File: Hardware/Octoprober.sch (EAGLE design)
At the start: 167 parts, among them J1 10118193-0001LF, SW1 EVQ-Q2203W, SW2 EVQ-Q2203W, SW3 EVQ-Q2203W, SW4 EVQ-Q2203W, SW5 EVQ-Q2203W, U1 P8X32A-M44, U10 DS1340Z-33+, U11 MCP3424-E/ST, U12 MCP3424-E/ST, U13 AT30TSE752-XM8-T, U14 AT30TSE752-XM8-T, U15 AT30TSE752-XM8-T, U16 AT30TSE752-XM8-T, U17 AT30TSE752-XM8-T, U18 AT30TSE752-XM8-T, U19 AT30TSE752-XM8-T, U2 CAT24C512WI-GT3, U20 AT30TSE752-XM8-T, U21 PMV22EN,215, U3 ADP3338AKCZ-3.3-RL, U4 FT230XQ-R, U5 BQ24075RGTT, U6 74HC2G04GV,125, U7 PMV22EN,215, U8 PMV160UP,215, U9 MCP3021A5T-E/OT, X1 ABLS3-6.000MHZ-D4Y-T, X2 ABS25-32.768KHz-1-T

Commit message: New chips for thermocouples.
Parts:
- removed C54: 1uF, PP_Passives:CAPACITOR_NON_POLAR0402
- removed FU: (no value), PP_Connectors:PH_1X09PTH
- removed J1: 10118193-0001LF, PP_Connectors:USB10118193-0001LF
- removed L10, L11, L12, L13, L14, L15, L16, L17, L3, L4, L5, L6, L7, L8, L9: BK1005HM471-T, PP_Passives:INDUCTOR0402
- removed LCD1: (no value), PP_Displays:HD44780_LCD1602_COUNTERSINK
- removed R36: 10K, PP_Passives:RESISTOR0402
- removed R37, R38: 560, PP_Passives:RESISTOR0402
- removed U20: AT30TSE752-XM8-T, PP_DigitalIC:AT30TSEXXXMSOP-8
- removed U21: PMV22EN,215, PP_DiscreteSemi:MOSFET_N-CHANNEL_SINGLESOT-23
- added C55, C58, C59, C60, C63, C64, C65, C68, C69, C70, C73, C74: 0.1uF, PP_Passives:CAPACITOR_NON_POLAR0402
- added C56, C57, C61, C62, C66, C67, C71, C72: 0.01uF, PP_Passives:CAPACITOR_NON_POLAR0402
- added FID1: GSM_FIDUCIAL, MF_Aesthetics:GSM_FIDUCIAL
- added J3: (no value), MF_Connectors:USB_MICRO_RIGHT
- added U$7: MF_LOGOLOGO_MEDIUM, PP_Aesthetics:MF_LOGOLOGO_MEDIUM
- C10, C11, C12, C13, C14, C2, C3, C34, C37, C38, C39, C4, C40, C5, C6, C9: device PP_Passives:CAPACITOR_NON_POLAR0402 -> PP_Passives:CAPACITOR_NON_POLAR0603
- C15, C21, C29, C49, C50: value 0.1uF -> 0.01uF
- C16, C18, C20, C24, C26, C28: value 0.01uF -> 0.1uF
- C17: value 10uF -> 0.01uF
- C19: value 10uF -> 0.1uF
- C41, C42, C43, C44: device PP_Passives:CAPACITOR_NON_POLAR0402 -> PP_Passives:CAPACITOR_NON_POLAR1206
- D1, D12, D2: device PP_LED:LED_SINGLE0402 -> PP_LED:LED_SINGLE0805
- L2: value BK1005HM471-T -> MI0603K300R-10; device PP_Passives:INDUCTOR0402 -> PP_Passives:RESISTOR0603
- R1, R10, R11, R12, R13, R14, R15, R16, R17, R18, R19, R20, R21, R22, R23, R24, R25, R26, R27, R28, R29, R30, R31, R32, R33, R34, R8, R9: device PP_Passives:RESISTOR0402 -> PP_Passives:RESISTOR0603
- SD1: value 502570-0893 -> (none); device PP_Connectors:SD_CARD502570-0893 -> MF_Connectors:SD_CARD_SLOT_MICRO_RIGHT
- U$1: REVNUM REV 2 -> REV 3
- U1: value P8X32A-M44 -> P8X32A-Q44; device PP_DigitalIC:P8X32A_PROPELLERQFN-44 -> MF_IC_Digital:P8X32A-Q44
- U11, U12: value MCP3424-E/ST -> MAX31856MUD+; device PP_DigitalIC:MCP3424TTSOP-14 -> PP_AnalogIC:MAX31856
- U13, U14, U15, U16, U17, U18: value AT30TSE752-XM8-T -> MAX31856MUD+; device PP_DigitalIC:AT30TSEXXXMSOP-8 -> PP_AnalogIC:MAX31856
- U19: value AT30TSE752-XM8-T -> IP4234CZ6,125; device PP_DigitalIC:AT30TSEXXXMSOP-8 -> PP_Passives:IP4234CZ6SOT-457
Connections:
- removed net LCD_CS: LCD1.BK_GND, U1.P7
- removed net LCD_SDI: LCD1.D7, U1.P6
- removed net LCD_SDO: LCD1.D6, U1.P5
- removed net N$10: D6.2, L7.P$1, TC3.2
- removed net N$11: D6.1, L6.P$2, TC3.1
- removed net N$12: D7.2, L9.P$1, TC4.2
- removed net N$13: D7.1, L8.P$2, TC4.1
- removed net N$14: D11.2, L17.P$1, TC8.2
- removed net N$15: D11.1, L16.P$2, TC8.1
- removed net N$16: D10.2, L15.P$1, TC7.2
- removed net N$17: D10.1, L14.P$2, TC7.1
- removed net N$18: D9.2, L13.P$1, TC6.2
- removed net N$19: D9.1, L12.P$2, TC6.1
- removed net N$2: D4.2, L2.P$1, TC1.2
- removed net N$20: D8.2, L11.P$1, TC5.2
- removed net N$21: D8.1, L10.P$2, TC5.1
- removed net N$28: R37.1, U21.DRAIN
- removed net N$7: D4.1, L3.P$2, TC1.1
- removed net N$8: D5.2, L5.P$1, TC2.2
- removed net N$9: D5.1, L4.P$2, TC2.1
- removed net P12: FU.3, U1.P12
- removed net P13: FU.4, U1.P13
- removed net P14: FU.5, U1.P14
- removed net P15: FU.6, U1.P15
- removed net P16: FU.7, U1.P16
- removed net P17: FU.8, U1.P17
- removed net P18: FU.9, U1.P18
- removed net SCL_ADC: U1.P9, U11.SCL, U12.SCL, U13.SCL, U14.SCL, U15.SCL, U16.SCL, U17.SCL, U18.SCL, U19.SCL, U20.SCL
- removed net SDA_ADC: U1.P10, U11.SDA, U12.SDA, U13.SDA, U14.SDA, U15.SDA, U16.SDA, U17.SDA, U18.SDA, U19.SDA, U20.SDA
- removed net SHT_DRAIN: R36.1, U1.P11, U21.GATE
- new net ADC_0_!CS: U1.P12, U11.!CS
- new net ADC_1_!CS: U1.P13, U12.!CS
- new net ADC_2_!CS: U1.P14, U13.!CS
- new net ADC_3_!CS: U1.P15, U14.!CS
- new net ADC_4_!CS: U1.P16, U15.!CS
- new net ADC_5_!CS: U1.P17, U16.!CS
- new net ADC_6_!CS: U1.P18, U17.!CS
- new net ADC_7_!CS: U1.P19, U18.!CS
- new net ADC_SCK: U1.P11, U11.SCK, U12.SCK, U13.SCK, U14.SCK, U15.SCK, U16.SCK, U17.SCK, U18.SCK
- new net ADC_SDI: U1.P9, U11.SDI, U12.SDI, U13.SDI, U14.SDI, U15.SDI, U16.SDI, U17.SDI, U18.SDI
- new net ADC_SDO: U1.P10, U11.SDO, U12.SDO, U13.SDO, U14.SDO, U15.SDO, U16.SDO, U17.SDO, U18.SDO
- new net LCD_SDA: U1.P5
- new net N$23: J3.D-, U19.I/O2A
- new net N$26: J3.D+, U19.I/O1A
- new net N$27: J3.SLD, L2.1
- new net P6: U1.P6
- new net P7: U1.P7
- net !SLEEP: no longer U1.P20
- net 3.3V: no longer C54.2, FU.1, LCD1.VCC, R36.2, R37.2, R38.1
- net 3.3V_ANALOG: now also C18.1, C24.1, C26.1, C46.1, C47.1, C51.1, C52.1, C58.1, C59.1, C63.1, C64.1, C68.1, C69.1, C73.1, C74.1, U11.AVDD, U11.DVDD, U12.AVDD, U12.DVDD, U13.AVDD, U13.DVDD, U14.AVDD, U14.DVDD, U15.AVDD, U15.DVDD, U16.AVDD, U16.DVDD, U17.AVDD, U17.DVDD, U18.AVDD, U18.DVDD; no longer C15.1, C17.1, C21.1, C29.2, C46.2, C47.2, C48.2, C49.2, C50.2, C51.2, C52.2, U11.VCC, U12.ADR0, U12.ADR1, U12.VCC, U13.VCC, U14.A0, U14.VCC, U15.A1, U15.VCC, U16.A0, U16.A1, U16.VCC, U17.A2, U17.VCC, U18.A0, U18.A2, U18.VCC, U19.A1, U19.A2, U19.VCC, U20.A0, U20.A1, U20.A2, U20.VCC
- net CHARGING: now also U1.P20; no longer U1.P19
- net D+: now also U19.I/O1B; no longer J1.D+
- net D-: now also U19.I/O2B; no longer J1.D-
- net GND: now also C18.2, C22.2, C24.2, C26.2, C29.2, C30.2, C46.2, C47.2, C49.2, C50.2, C51.2, C52.2, C56.2, C57.2, C58.2, C59.2, C61.2, C62.2, C63.2, C64.2, C66.2, C67.2, C68.2, C69.2, C71.2, C72.2, C73.2, C74.2, J3.GND, L2.2, U11.AGND, U11.DGND, U12.AGND, U12.DGND, U13.AGND, U13.DGND, U14.AGND, U14.DGND, U15.AGND, U15.DGND, U16.AGND, U16.DGND, U17.AGND, U17.DGND, U18.AGND, U18.DGND; no longer C29.1, C46.1, C47.1, C48.1, C49.1, C50.1, C51.1, C52.1, C54.1, FU.2, J1.GND, LCD1.VSS, R38.2, U11.ADR0, U11.ADR1, U11.VDD, U12.VDD, U13.A0, U13.A1, U13.A2, U13.GND, U14.A1, U14.A2, U14.GND, U15.A0, U15.A2, U15.GND, U16.A2, U16.GND, U17.A0, U17.A1, U17.GND, U18.A1, U18.GND, U19.A0, U20.GND, U21.SOURCE
- net LCD_SCL: no longer LCD1.D5
- net TP_T+_0: now also C17.1, D4.1, TC1.1, U11.T+; no longer L3.P$1, U11.CH1+
- net TP_T+_1: now also C20.2, C22.1, D5.1, TC2.1, U12.T+; no longer C18.2, L4.P$1, U11.CH2+
- net TP_T+_2: now also C28.2, C30.1, D6.1, TC3.1, U13.T+; no longer C20.2, L6.P$1, U11.CH3+
- net TP_T+_3: now also C48.2, C50.1, D7.1, TC4.1, U14.T+; no longer C22.2, L8.P$1, U11.CH4+
- net TP_T+_4: now also C55.2, C57.1, D8.1, TC5.1, U15.T+; no longer C24.2, L10.P$1, U12.CH1+
- net TP_T+_5: now also C60.2, C62.1, D9.1, TC6.1, U16.T+; no longer C26.2, L12.P$1, U12.CH2+
- net TP_T+_6: now also C65.2, C67.1, D10.1, TC7.1, U17.T+; no longer C28.2, L14.P$1, U12.CH3+
- net TP_T+_7: now also C70.2, C72.1, D11.1, TC8.1, U18.T+; no longer C30.2, L16.P$1, U12.CH4+
- net TP_T-_0: now also C15.1, D4.2, TC1.2, U11.BIAS, U11.T-; no longer L2.P$2, U11.CH1-
- net TP_T-_1: now also C20.1, C21.1, D5.2, TC2.2, U12.BIAS, U12.T-; no longer C18.1, L5.P$2, U11.CH2-
- net TP_T-_2: now also C28.1, C29.1, D6.2, TC3.2, U13.BIAS, U13.T-; no longer C20.1, L7.P$2, U11.CH3-
- net TP_T-_3: now also C48.1, C49.1, D7.2, TC4.2, U14.BIAS, U14.T-; no longer C22.1, L9.P$2, U11.CH4-
- net TP_T-_4: now also C55.1, C56.1, D8.2, TC5.2, U15.BIAS, U15.T-; no longer C24.1, L11.P$2, U12.CH1-
- net TP_T-_5: now also C60.1, C61.1, D9.2, TC6.2, U16.BIAS, U16.T-; no longer C26.1, L13.P$2, U12.CH2-
- net TP_T-_6: now also C65.1, C66.1, D10.2, TC7.2, U17.BIAS, U17.T-; no longer C28.1, L15.P$2, U12.CH3-
- net TP_T-_7: now also C70.1, C71.1, D11.2, TC8.2, U18.BIAS, U18.T-; no longer C30.1, L17.P$2, U12.CH4-
- net USB_V0: now also J3.5V, U19.VB; no longer J1.5V
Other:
- moved on the sheet: C15, C16, C17, C18, C19, C20, C21, C22, C24, C26, C28, C29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

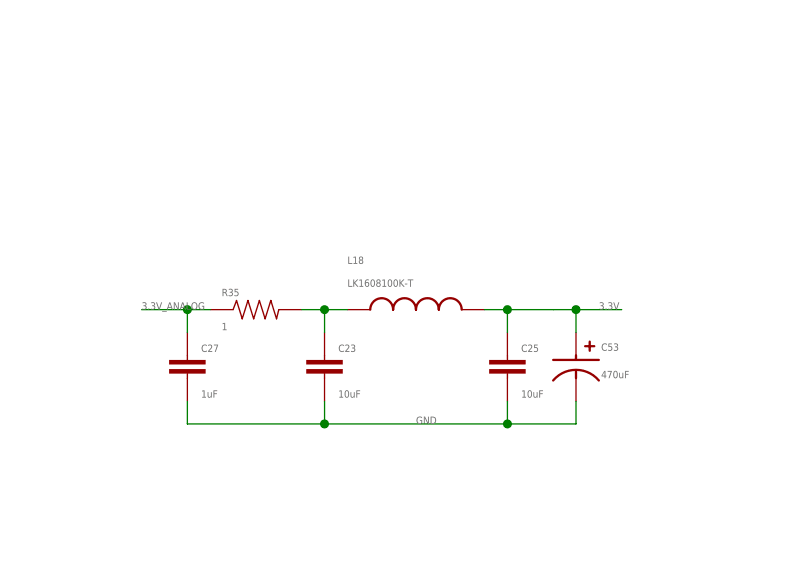
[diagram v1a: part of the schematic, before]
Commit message: Working on LCD setup. Need to find a case.
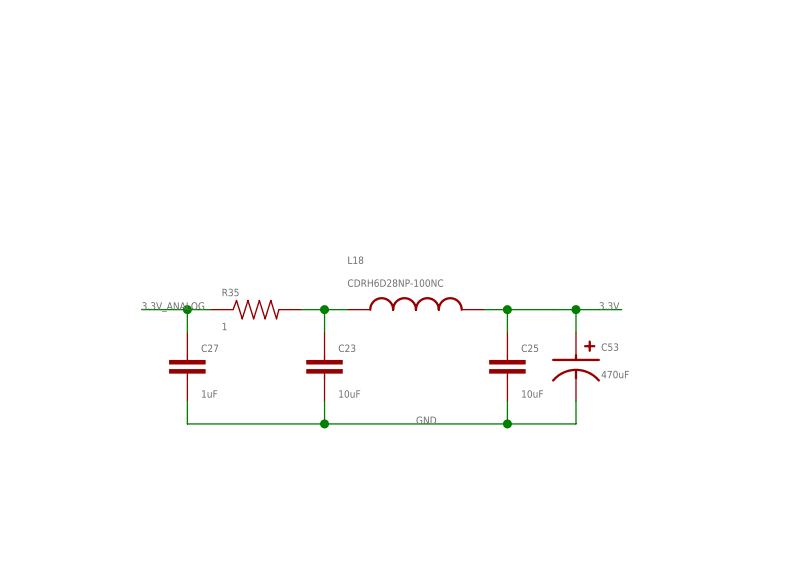
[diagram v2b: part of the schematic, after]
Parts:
- C23, C25: device PP_Passives:CAPACITOR_NON_POLAR0402 -> PP_Passives:CAPACITOR_NON_POLAR1206
- C27: device PP_Passives:CAPACITOR_NON_POLAR0402 -> PP_Passives:CAPACITOR_NON_POLAR0603
- L18: value LK1608100K-T -> CDRH6D28NP-100NC; device PP_Passives:INDUCTOR0603 -> PP_Passives:INDUCTORCDRH6D28
- R35: device PP_Passives:RESISTOR0402 -> PP_Passives:RESISTOR0603
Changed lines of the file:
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@@
 <part name="C44" library="PP_Passives" deviceset="CAPACITOR_NON_POLAR" device="1206" value="10uF"/>
 <part name="C45" library="PP_Passives" deviceset="CAPACITOR_POLARIZED" device="CASE_D" value="470uF"/>
-<part name="C23" library="PP_Passives" deviceset="CAPACITOR_NON_POLAR" device="0402" value="10uF"/>
-<part name="C25" library="PP_Passives" deviceset="CAPACITOR_NON_POLAR" device="0402" value="10uF"/>
-<part name="C27" library="PP_Passives" deviceset="CAPACITOR_NON_POLAR" device="0402" value="1uF"/>
-<part name="R35" library="PP_Passives" deviceset="RESISTOR" device="0402" value="1"/>
-<part name="L18" library="PP_Passives" deviceset="INDUCTOR" device="0603" value="LK1608100K-T"/>
+<part name="C23" library="PP_Passives" deviceset="CAPACITOR_NON_POLAR" device="1206" value="10uF"/>
+<part name="C25" library="PP_Passives" deviceset="CAPACITOR_NON_POLAR" device="1206" value="10uF"/>
+<part name="C27" library="PP_Passives" deviceset="CAPACITOR_NON_POLAR" device="0603" value="1uF"/>
+<part name="R35" library="PP_Passives" deviceset="RESISTOR" device="0603" value="1"/>
+<part name="L18" library="PP_Passives" deviceset="INDUCTOR" device="CDRH6D28" value="CDRH6D28NP-100NC"/>
 <part name="C53" library="PP_Passives" deviceset="CAPACITOR_POLARIZED" device="CASE_D" value="470uF"/>
 <part name="U11" library="PP_AnalogIC" deviceset="MAX31856" device="" value="MAX31856MUD+"/>

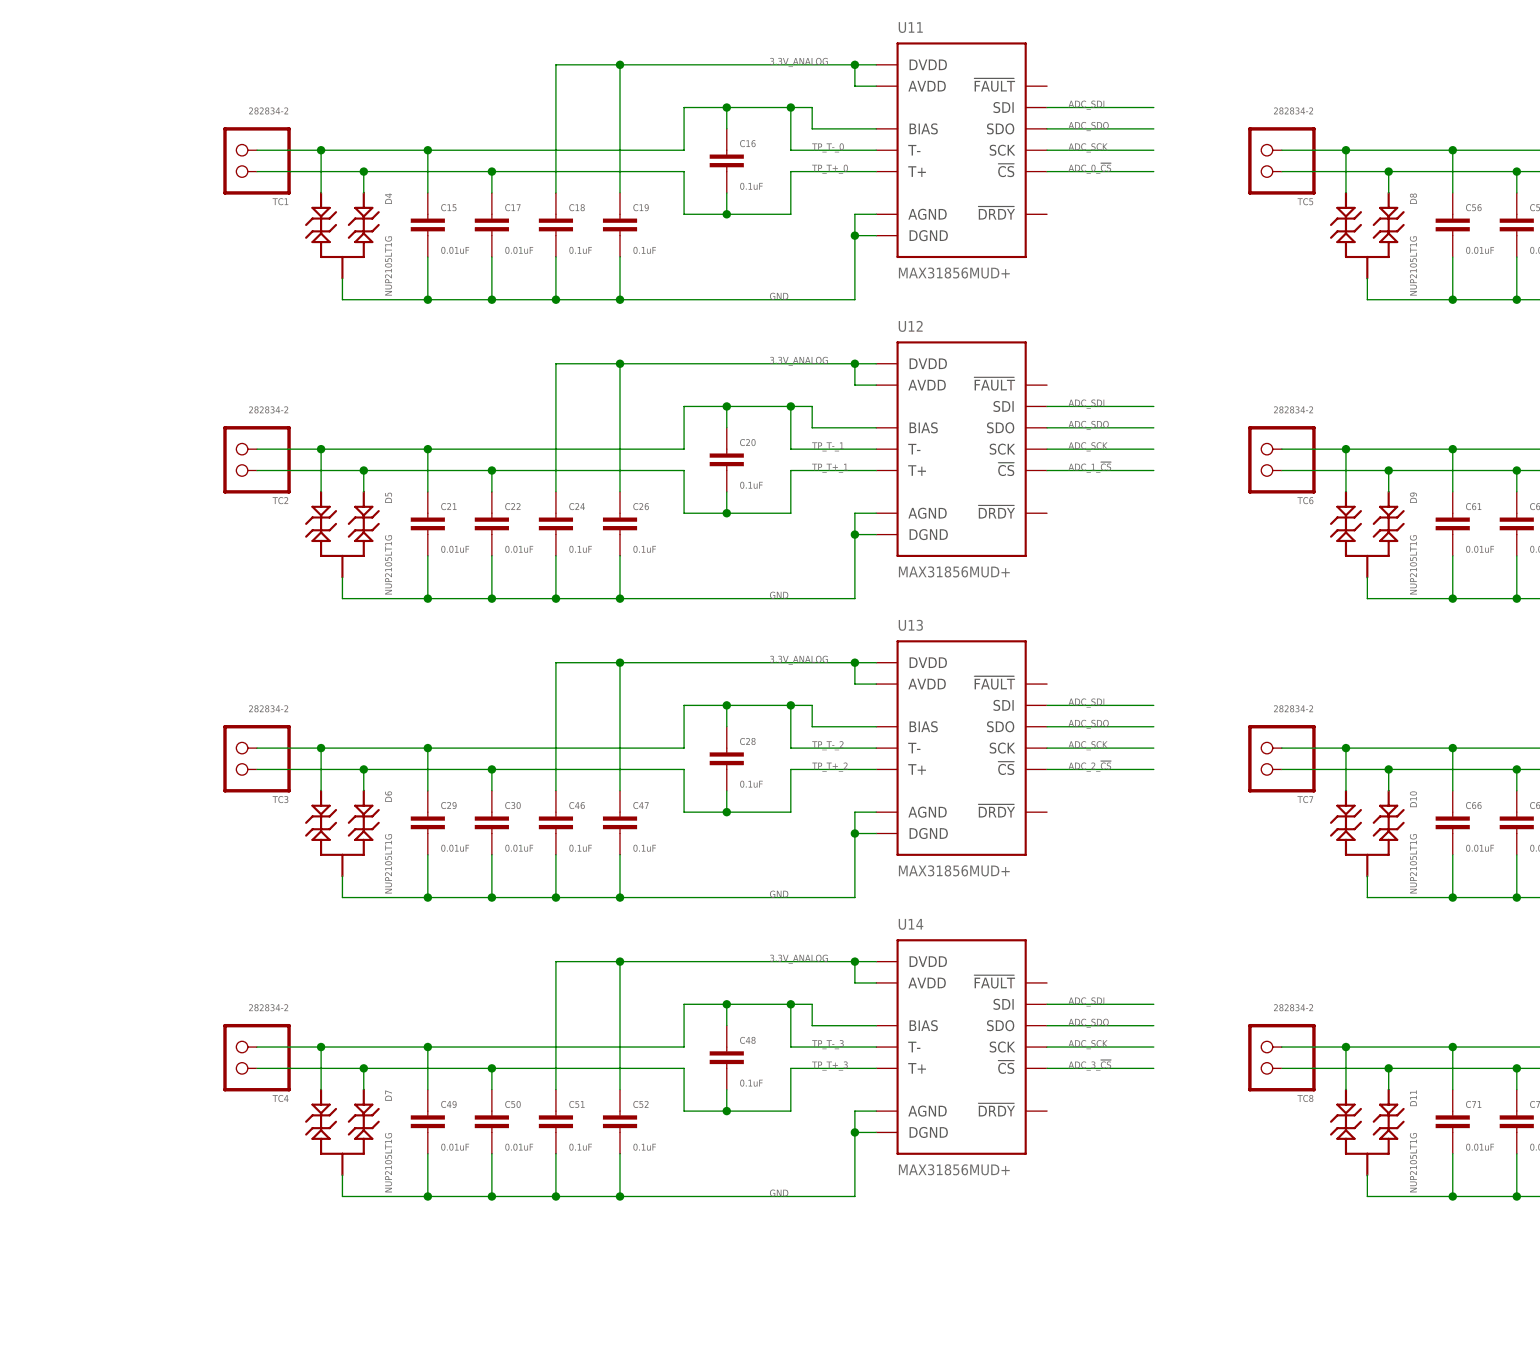
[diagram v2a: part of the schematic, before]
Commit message: Thermocouple connectors added.
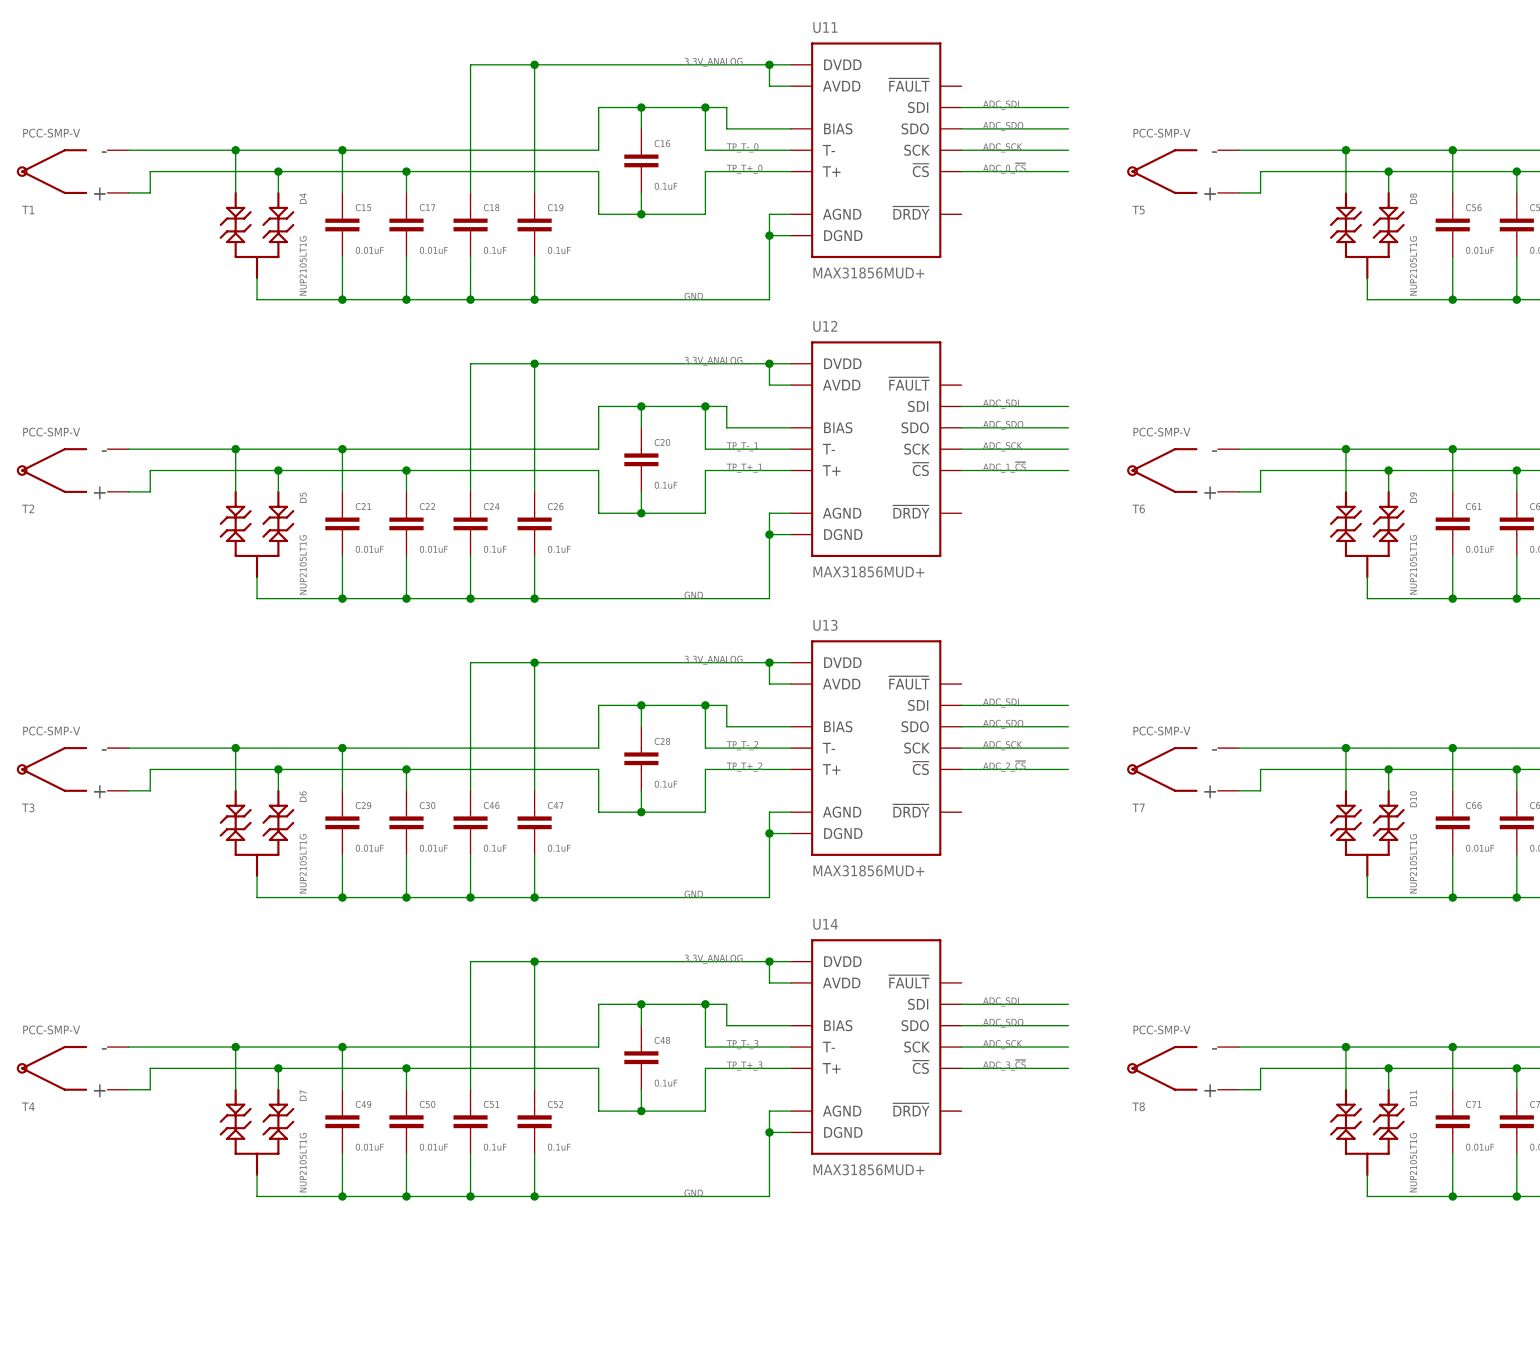
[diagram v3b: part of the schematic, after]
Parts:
- removed TC1, TC2, TC3, TC4, TC5, TC6, TC7, TC8: 282834-2, PP_Connectors:PH_1X02SCREW_TERM
- added T1, T2, T3, T4, T5, T6, T7, T8: PCC-SMP-V, PP_Connectors:THERMOCOUPLE_CONPCC-SMP-V
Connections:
- net TP_T+_0: now also T1.POS; no longer TC1.1
- net TP_T+_1: now also T2.POS; no longer TC2.1
- net TP_T+_2: now also T3.POS; no longer TC3.1
- net TP_T+_3: now also T4.POS; no longer TC4.1
- net TP_T+_4: now also T5.POS; no longer TC5.1
- net TP_T+_5: now also T6.POS; no longer TC6.1
- net TP_T+_6: now also T7.POS; no longer TC7.1
- net TP_T+_7: now also T8.POS; no longer TC8.1
- net TP_T-_0: now also T1.NEG; no longer TC1.2
- net TP_T-_1: now also T2.NEG; no longer TC2.2
- net TP_T-_2: now also T3.NEG; no longer TC3.2
- net TP_T-_3: now also T4.NEG; no longer TC4.2
- net TP_T-_4: now also T5.NEG; no longer TC5.2
- net TP_T-_5: now also T6.NEG; no longer TC6.2
- net TP_T-_6: now also T7.NEG; no longer TC7.2
- net TP_T-_7: now also T8.NEG; no longer TC8.2
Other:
- moved on the sheet: C15, C16, C17, C18, C19, C20, C21, C22, C24, C26, C28, C29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

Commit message: Switched display to a ERC128128FS
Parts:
- added C54: 10uF, PP_Passives:CAPACITOR_NON_POLAR1206
- added C75: 0.01uF, PP_Passives:CAPACITOR_NON_POLAR0603
- added C76, C77, C78, C79: 1uF, PP_Passives:CAPACITOR_NON_POLAR0603
- added C80: 3.3uF, PP_Passives:CAPACITOR_NON_POLAR0603
- added J1: ER-CON2.0-2P-SMD, PP_Connectors:PH_1X02ER-CON2.0-2P-SMD
- added J4: ER-CON31HT-1, PP_Connectors:ER-CON31HT-1
- added R36, R37: 22, PP_Passives:RESISTOR0603
- added R38, R39: 10K, PP_Passives:RESISTOR0603
- added U20: PMV160UP,215, PP_DiscreteSemi:MOSFET_P-CHANNEL_SINGLESOT-23
- C15, C16, C17, C18, C19, C20, C21, C22, C24, C26, C28, C29, C30, C46, C47, C48, C49, C50, C51, C52, C55, C56, C57, C58, C59, C60, C61, C62, C63, C64, C65, C66, C67, C68, C69, C70, C71, C72, C73, C74: device PP_Passives:CAPACITOR_NON_POLAR0402 -> PP_Passives:CAPACITOR_NON_POLAR0603
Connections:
- removed net P6: U1.P6
- removed net P7: U1.P7
- new net A: J1.1, R36.2
- new net LCD_BKLT: R37.1, U1.P7, U20.GATE
- new net LCD_RST: J4.PIN5, U1.P6
- new net N$10: C79.1, J4.PIN27
- new net N$11: C78.1, J4.PIN28
- new net N$12: C77.1, J4.PIN29
- new net N$13: C76.1, J4.PIN30
- new net N$14: C76.2, C77.2, C78.2, C79.2, C80.2
- new net N$2: C54.1, C75.1, J4.PIN17, J4.PIN18, J4.PIN19, J4.PIN20
- new net N$7: R36.1, U20.DRAIN
- new net N$8: C54.2, C75.2, J4.PIN21, J4.PIN22, J4.PIN23, J4.PIN24
- new net N$9: C80.1, J4.PIN25
- net 3.3V: now also J4.PIN10, J4.PIN26, J4.PIN3, J4.PIN4, J4.PIN6, J4.PIN7, J4.PIN8, J4.PIN9, R37.2, R38.2, R39.2, U20.SOURCE
- net GND: now also J1.2, J4.PIN1, J4.PIN2
- net LCD_SCL: now also J4.PIN11, J4.PIN12, J4.PIN13, J4.PIN15, R38.1
- net LCD_SDA: now also J4.PIN16, R39.1
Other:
- moved on the sheet: R21, R22, R23, SW2, SW3, SW4
